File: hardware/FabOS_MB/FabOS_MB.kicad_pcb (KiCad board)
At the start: 4 copper layers, 68 x 68 mm, 116 parts, among them J201 USB_A, J301 RJ45, J401 USB_C_Receptacle, J601 Conn_ST_STDC14, SW601 boot, SW602 SW_Push, SW603 SW_Push, SW604 SW_Push, SW605 SW_Push, U201 NCV7329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

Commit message: update footprint
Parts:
- C202, C615: footprint Capacitor_SMD:C_0402_1005Metric_Pad0.74x0.62mm_HandSolder -> Capacitor_SMD:C_0402_1005Metric
- C303, C305: value 30p -> 20p
- H101, H102, H103, H104: footprint MountingHole:MountingHole_3.2mm_M3_DIN965_Pad -> MountingHole:MountingHole_3.2mm_M3_Pad_Via
- JP501: footprint Jumper:SolderJumper-2_P1.3mm_Open_Pad1.0x1.5mm -> Jumper:SolderJumper-2_P1.3mm_Open_TrianglePad1.0x1.5mm
- R601: footprint Resistor_SMD:R_0402_1005Metric_Pad0.72x0.64mm_HandSolder -> Resistor_SMD:R_0402_1005Metric

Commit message: Placement des composants
On va mourir
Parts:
- C201, C310, C502, C503: footprint Capacitor_SMD:C_Elec_4x5.4 -> Capacitor_SMD:C_0402_1005Metric
- C505, C506: footprint Capacitor_SMD:C_Elec_6.3x5.4 -> Capacitor_SMD:C_0201_0603Metric_Pad0.64x0.40mm_HandSolder
- moved C505 149.1 mm to (168.9, 127.8)
- moved SW602 149.1 mm to (144.7, 159.3)
- moved C506 142.7 mm to (169.7, 121.0)
- moved SW601 142.7 mm to (137.0, 148.8)
- moved C502 135.3 mm to (168.4, 115.0)
- moved SW603 131.6 mm to (121.2, 159.3), turned to 180 degrees
- moved C503 131.2 mm to (171.6, 104.9)
- moved SW604 129.9 mm to (132.5, 159.4), turned to 180 degrees
- moved C201 126.8 mm to (160.2, 109.7), turned to -90 degrees
- moved JP501 125.2 mm to (134.8, 113.1)
- moved U502 119.3 mm to (153.2, 114.2)
- moved SW605 113.1 mm to (109.6, 159.2)
- moved D501 112.1 mm to (147.8, 116.1), turned to 180 degrees
- moved D502 109.0 mm to (147.8, 113.9), turned to 180 degrees
- moved U401 107.7 mm to (151.4, 107.3), turned to -90 degrees
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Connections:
- C310 pad 1: /ethernet/CT -> GND
- C310 pad 2: GND -> /ethernet/CT
- U601 pad 17: /LIN_EN -> unconnected-(U601-PC2-Pad17)
- U601 pad 31: unconnected-(U601-PA6-Pad31) -> /NRST_ETH
- U601 pad 68: /USART1_TX -> unconnected-(U601-PA9-Pad68)
- U601 pad 69: /USART1_TX -> unconnected-(U601-PA10-Pad69)
- U601 pad 7: /NRST_ETH -> unconnected-(U601-PC13-Pad7)
- U601 pad 90: unconnected-(U601-PB4-Pad90) -> /LIN_EN
- U601 pad 92: unconnected-(U601-PB6-Pad92) -> /USART1_TX
- U601 pad 93: unconnected-(U601-PB7-Pad93) -> /USART1_TX

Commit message: update pcb
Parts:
- moved C607 120.3 mm to (122.5, 151.1), turned to -90 degrees
- moved C609 117.0 mm to (123.5, 151.1), turned to -90 degrees
- moved C610 115.6 mm to (124.6, 151.1), turned to -90 degrees
- moved C604 114.4 mm to (118.5, 151.1), turned to -90 degrees
- moved C606 109.9 mm to (116.0, 151.2), turned to -90 degrees
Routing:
- net +3.3V: track 0.00 -> 11.1 mm, vias 0 -> 5
- net GND: track 0.00 -> 10.1 mm, vias 0 -> 4

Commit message: update
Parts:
- moved C613 118.3 mm to (130.0, 147.0)
- moved C614 115.5 mm to (130.0, 145.8)
- moved C618 112.1 mm to (130.0, 148.0)
- moved C602 109.1 mm to (130.5, 135.5)
- moved C615 108.7 mm to (126.0, 151.0), turned to -90 degrees
- moved C611 104.4 mm to (109.0, 146.8), turned to 180 degrees
- moved C617 102.0 mm to (130.5, 134.5)
- moved C608 97.5 mm to (117.5, 130.5), turned to 90 degrees
- moved C202 88.2 mm to (107.5, 132.0)
- moved R602 87.4 mm to (118.5, 130.5), turned to 90 degrees
- moved C201 56.9 mm to (107.5, 131.0), turned to 0 degrees
- moved U301 3.22 mm to (125.5, 127.0), turned to -90 degrees
- moved U303 0.30 mm to (117.8, 126.0)
- moved U601 0.12 mm to (119.5, 140.7)
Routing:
- net Net-(R602-Pad2): track 0.00 -> 37.6 mm, vias 0 -> 2
- net /5V_USB: track 0.00 -> 16.6 mm
- net GND: track 10.1 -> 26.5 mm, vias 4 -> 12
- net +3.3V: track 11.1 -> 23.8 mm, vias 5 -> 9
- net /STM32/BTN1: track 0.00 -> 3.07 mm
- net Net-(U601-VCAP_1): track 0.00 -> 2.95 mm

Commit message: paire diff?
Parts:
- moved J601 23.2 mm to (172.8, 142.5)
- moved J301 14.2 mm to (151.2, 129.0)
- moved U303 11.0 mm to (128.3, 129.5)
- moved U301 7.00 mm to (119.4, 123.6)
- moved C310 3.62 mm to (133.7, 140.3)
- moved U302 2.19 mm to (136.5, 133.1)
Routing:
- net /ethernet/TD-: track 0.00 -> 16.7 mm
- net /ethernet/TD+: track 0.00 -> 15.3 mm
- net /ethernet/RX+: track 0.00 -> 9.38 mm
- net /ethernet/RX-: track 0.00 -> 8.70 mm
- net /ethernet/TX-: track 0.00 -> 7.28 mm
- net /ethernet/TX+: track 0.00 -> 6.77 mm

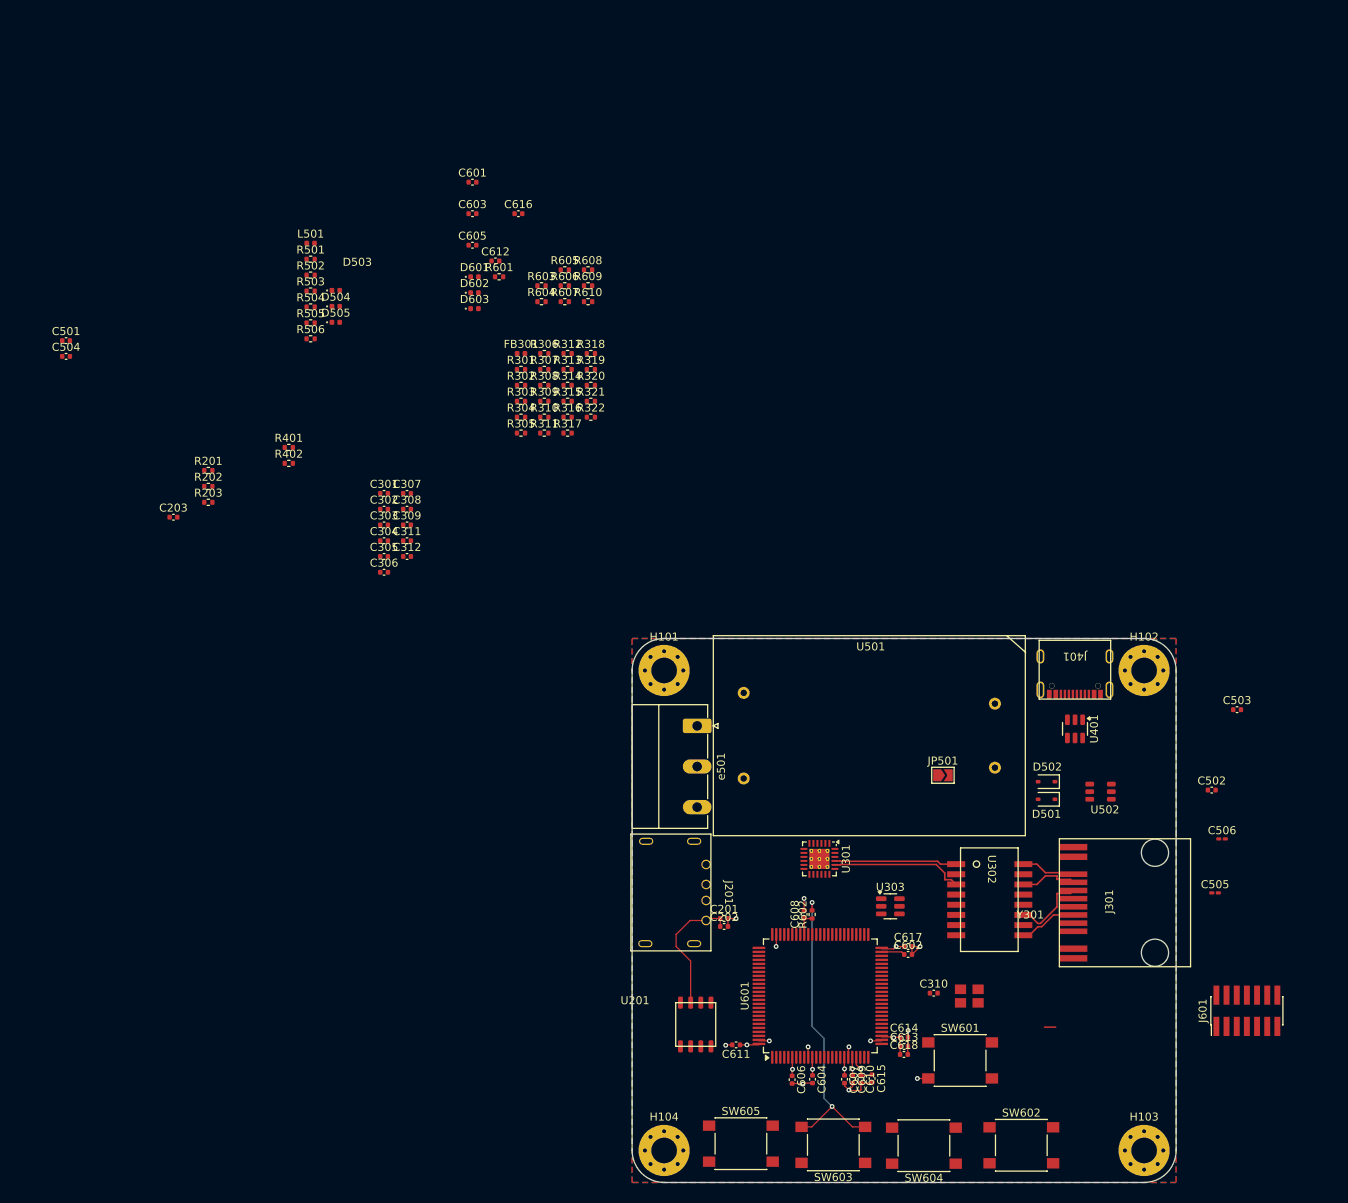
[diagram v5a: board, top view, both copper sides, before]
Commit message: update components placement
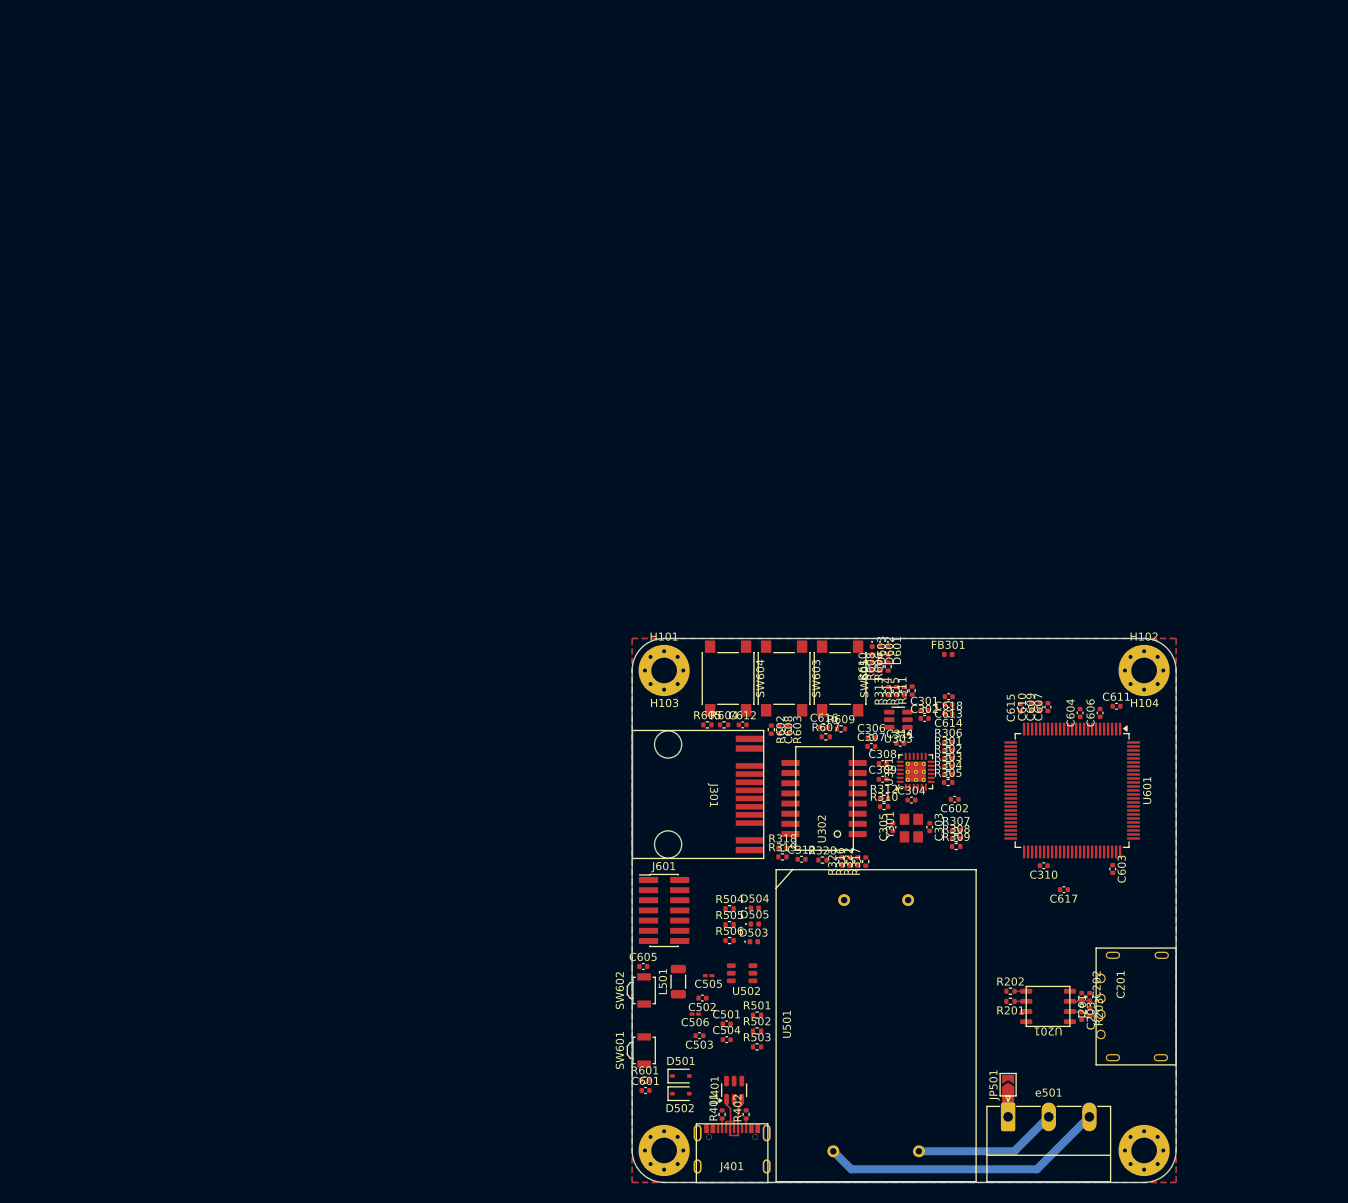
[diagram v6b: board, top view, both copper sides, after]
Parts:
- L501: footprint Inductor_SMD:L_0402_1005Metric -> Inductor_SMD:L_1206_3216Metric
- SW601, SW602: footprint Button_Switch_SMD:SW_Push_1P1T_NO_6x6mm_H9.5mm -> Button_Switch_SMD:SW_SPST_B3U-3000P
- moved C203 129.5 mm to (152.2, 143.2), turned to -90 degrees
- moved R203 127.3 mm to (153.2, 142.7), turned to -90 degrees
- moved R201 120.2 mm to (143.3, 141.4), turned to 180 degrees
- moved C501 118.8 mm to (107.8, 144.2)
- moved C504 118.8 mm to (107.8, 146.2)
- moved R202 118.5 mm to (143.3, 140.1)
- moved C601 115.6 mm to (97.7, 152.5)
- moved C603 114.5 mm to (156.1, 124.8), turned to -90 degrees
- moved R502 109.7 mm to (111.6, 145.1)
- moved R503 109.7 mm to (111.6, 147.1)
- moved R501 109.7 mm to (111.6, 143.1)
- moved L501 103.1 mm to (101.8, 138.9), turned to 90 degrees
- moved R601 102.1 mm to (97.6, 151.2)
- moved R402 99.5 mm to (110.2, 155.5), turned to 90 degrees
- moved R401 99.4 mm to (107.2, 155.5), turned to 90 degrees
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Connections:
- C201 pad 1: /5V_USB -> /5V_Flyback
- C202 pad 1: /5V_USB -> /5V_Flyback
- D501 pad 2: /power/5V_Flyback -> /5V_Flyback
- J201 pad 1: /5V_USB -> /5V_Flyback
- R203 pad 1: /5V_USB -> /5V_Flyback
- R506 pad 1: /power/5V_Flyback -> /5V_Flyback
- U201 pad 7: /5V_USB -> /5V_Flyback
- U401 pad 1: /USB_C/D+ -> /USB_C/D-
- U401 pad 3: /USB_C/D- -> /USB_C/D+
- U401 pad 4: /USB_DM -> /USB_DP
- U401 pad 6: /USB_DP -> /USB_DM
- U501 pad 6: /power/5V_Flyback -> /5V_Flyback
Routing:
- net Net-(R602-Pad2): track 37.6 -> 0.00 mm, vias 2 -> 0
- net L: track 0.00 -> 35.7 mm
- net GND: track 26.5 -> 0.00 mm, vias 12 -> 0
- net +3.3V: track 23.8 -> 0.00 mm, vias 9 -> 0
- net N: track 0.00 -> 18.0 mm
- net /ethernet/TD-: track 16.7 -> 0.00 mm
- net /5V_USB: track 16.6 -> 0.00 mm
- net /ethernet/TD+: track 15.3 -> 0.00 mm
- net /ethernet/RX+: track 9.38 -> 0.00 mm
- net /ethernet/RX-: track 8.70 -> 0.00 mm
- net /ethernet/TX-: track 7.28 -> 0.00 mm
- net /ethernet/TX+: track 6.77 -> 0.00 mm
- net /USB_C/D+: track 0.00 -> 6.53 mm
- net /USB_C/D-: track 0.00 -> 5.67 mm
- net /LIN/LIN: track 0.00 -> 4.20 mm
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- added copper zone on In2.Cu, net /5V_Flyback

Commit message: update librairies
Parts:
- Y301: footprint Librairie_MB:Oscillateur crystal 4p -> Crystal:Crystal_SMD_3225-4Pin_3.2x2.5mm

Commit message: update pcb
C'est la merde
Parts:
- removed C306: 100n, Capacitor_SMD:C_0402_1005Metric
- moved R321 46.2 mm to (158.9, 151.9)
- moved C312 46.2 mm to (153.9, 151.6)
- moved R316 46.2 mm to (159.9, 151.9)
- moved R317 46.2 mm to (161.9, 151.9)
- moved R319 46.2 mm to (151.5, 151.3)
- moved R320 46.2 mm to (156.5, 151.7)
- moved C304 34.6 mm to (162.1, 131.2)
- moved Y301 32.9 mm to (148.6, 147.5)
- moved C311 32.6 mm to (154.2, 130.3)
- moved C307 32.6 mm to (150.6, 130.7)
- moved R322 30.4 mm to (152.3, 135.4)
- moved R318 29.9 mm to (144.6, 124.8)
- moved C602 28.9 mm to (161.8, 129.8)
- moved R310 23.4 mm to (144.1, 133.5)
- moved R312 23.3 mm to (144.0, 132.4)
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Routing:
- net /ethernet/TD+: track 0.00 -> 36.4 mm
- net /ethernet/TD-: track 0.00 -> 33.8 mm
- net GND: track 0.00 -> 11.3 mm, vias 0 -> 3
- net /ethernet/RX+: track 0.00 -> 10.6 mm
- net /ethernet/RX-: track 0.00 -> 10.6 mm
- net /ethernet/TX-: track 0.00 -> 9.50 mm
- net /ethernet/TX+: track 0.00 -> 9.50 mm
- net /ethernet/RD+: track 0.00 -> 7.61 mm
- net /ethernet/RD-: track 0.00 -> 7.61 mm
- net /ethernet/CT: track 0.00 -> 3.94 mm
- net /ethernet/VDDCR: track 0.00 -> 3.01 mm, vias 0 -> 1
- net Net-(U301-~{INT}/REFCLKO): track 0.00 -> 2.65 mm
- net /ETH_RXD1: track 0.00 -> 1.57 mm, vias 0 -> 1
- net /ETH_REF_CLK: track 0.00 -> 1.54 mm, vias 0 -> 1
- net /ETH_TX_EN: track 0.00 -> 1.50 mm, vias 0 -> 1
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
